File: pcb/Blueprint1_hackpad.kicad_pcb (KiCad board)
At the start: 2 copper layers, 86 x 71 mm, 18 parts, among them SW1 SW_Push, SW2 SW_Push, SW3 SW_Push, SW4 SW_Push, SW5 SW_Push, SW6 SW_Push, SW7 SW_Push, SW8 SW_Push, U1 XIAO-RP2040-DIP

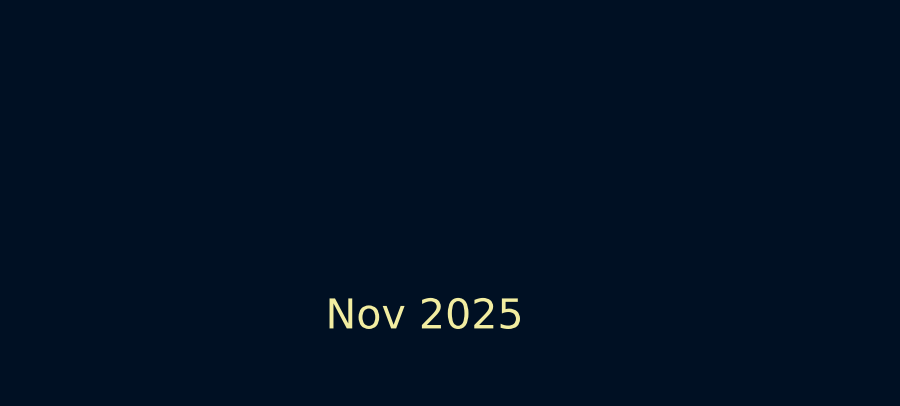
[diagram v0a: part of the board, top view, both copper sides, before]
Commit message: added case
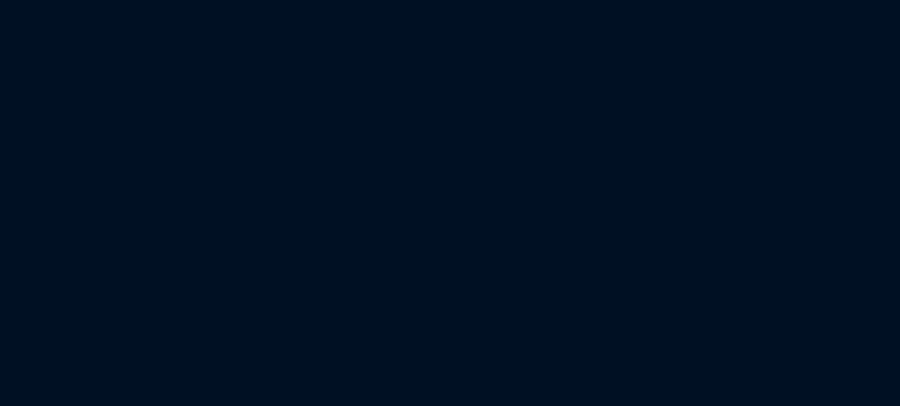
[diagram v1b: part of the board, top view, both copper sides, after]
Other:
- board text removed: "Nov 2025"
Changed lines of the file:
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@@
 		(layer "Edge.Cuts")
-	)
-	(gr_text "Nov 2025"
-		(at 93 165.5 0)
-		(layer "F.SilkS")
-		(effects
-			(font
-				(size 1 1)
-				(thickness 0.15)
-			)
-			(justify left bottom)
-		)
 	)
 	(gr_text "Blueprint Nov 2025\n"
